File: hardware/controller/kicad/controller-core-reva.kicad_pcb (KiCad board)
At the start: 2 copper layers, 141.6 x 135.2 mm, 158 parts, among them J101 12V_ISOLATED_INPUT / JST XH, J102 STM_SWD / 1x6 2.54mm, J103 ESP_UART / 1x6 2.54mm, J104 UI_LINK / IDC 2x8 2.54mm, J105 JP13 NTC / 2 vías, J106 JP5 FLOW ADAPTER / VCC-GND-OC, J107 JP14 DOOR / contacto seco, J108 JP16 VISUAL V1..V8 / XH-8, J109 JP22 WATER / RED-WHITE-BLACK, J110 USB-C SERVICE / USB 2.0, J111 USB BENCH POWER / OPEN, J112 24V_ACTUATOR_INPUT / JST XH, J113 JP3 VALVE / JST XH, J114 POWER MONITOR / MEASURE ONLY, J115 JP8 GRINDER / 320VDC, J117 JP24 PUMP / 230VAC, J118 JP17 MAINS / L-N, J121 24V INTERNAL SELECT / OPEN FO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, K701 G5RL-1A-E-TV8 DC24, Q501 SI2308A, Q701 SI2308A / relay coil, U101 STM32G431RBT6, U201 ESP32-S3-WROOM-1U-N8R8, U203 USBLC6-2SC6, U301 AP63203WU-7, U302 TPS22918DBVR, U303 AP63200WU-7 / 24V to 12V, U501 DRV8876PWPR, U502 UCC27517DBVR, U601 TPS3828-33DBVR, U602 SN74LVC2G08DCTR, U603 SN74LVC2G08DCTR

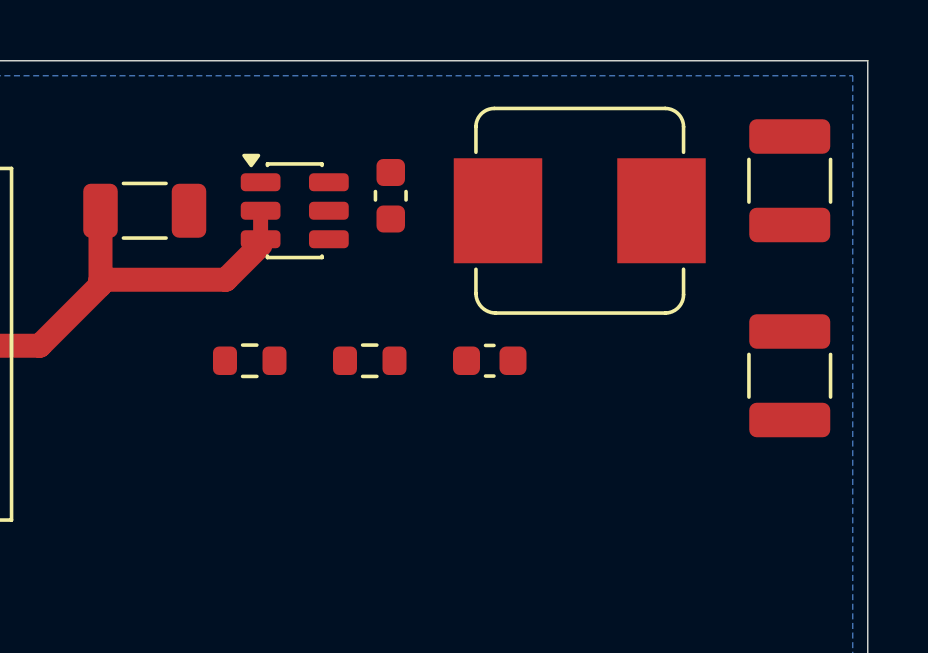
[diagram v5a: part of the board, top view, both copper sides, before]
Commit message: Route the 12 V buck and document the routed blocks
Route the switch node, output bank and divider chain of the AP63200 stage; the
1210 output capacitors share a column with a ground pad, so the rail rounds
them on the inner side. Leave the feedback leg from U303 pin 1 to R302 open and
say why: the 24 V lane wraps round C310 to reach the input pins, leaving only
the channel under the switcher, next to the switch node.

Document every hand-routed block, the reserved reset channel, the back-layer
hops under the power trunks, and two findings: U603 has no decoupling capacitor
of its own, and the SN74LVC2G08 in the DCT package really does carry 2Y on pin
3, which the generator's symbol already matches. DRC clean; 155 connections
remain, down from 273.

Co-Authored-By: Claude Opus 5 <noreply@anthropic.com>
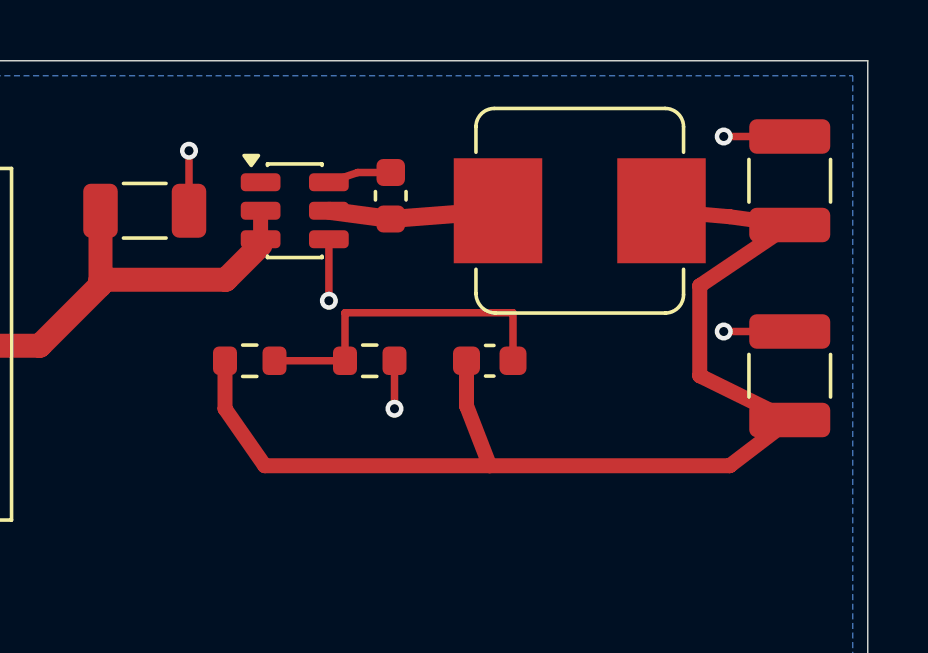
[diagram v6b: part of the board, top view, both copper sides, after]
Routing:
- net /12V_ISO_RAW: track 0.00 -> 39.4 mm
- net /BUCK12_FB: track 0.00 -> 11.2 mm
- net /GND_UI: track 91.9 -> 102.0 mm, vias 56 -> 61
- net /BUCK12_SW: track 0.00 -> 5.67 mm
- net /BUCK12_BST: track 0.00 -> 2.12 mm

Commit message: Give U603 decoupling and the 12 V feedback a clean path
Add C603, a 100 nF beside U603 between it and Q701. The gate that arms mains
was the only logic part without local decoupling, so a supply dip could have
read as a valid high on its inputs.

Move the 12 V feedback divider from below the switcher to the top edge,
north-west of it. Below the switcher it had no route at all: the 24 V lane
wraps round C310 at y = 7.3 mm to reach the input pins, leaving only the
0.95 mm channel under the chip, beside the switch node. R302, R303 and C314 now
share one line at y = 3.4 mm into pin 1 that never meets the lane, and the
divider's top end returns to the inductor pad on a no-current sense line along
the board edge.

ERC passes at 159 components. DRC clean; 154 connections remain.

Co-Authored-By: Claude Opus 5 <noreply@anthropic.com>
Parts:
- added C603: 100nF / arm gate local, Capacitor_SMD:C_0603_1608Metric, F.Cu at (31.5, 75.6)
- moved R303 18.7 mm to (108.0, 2.20), turned to 180 degrees
- moved C314 14.3 mm to (117.0, 2.20)
- moved R302 11.2 mm to (113.0, 2.20)
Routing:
- net /BUCK12_FB: track 11.2 -> 14.4 mm
- net /3V3_CORE: track 83.8 -> 85.6 mm
- net /12V_ISO_RAW: track 39.4 -> 40.9 mm
- net /GND_UI: track 102.0 -> 102.4 mm, vias 61 -> 62

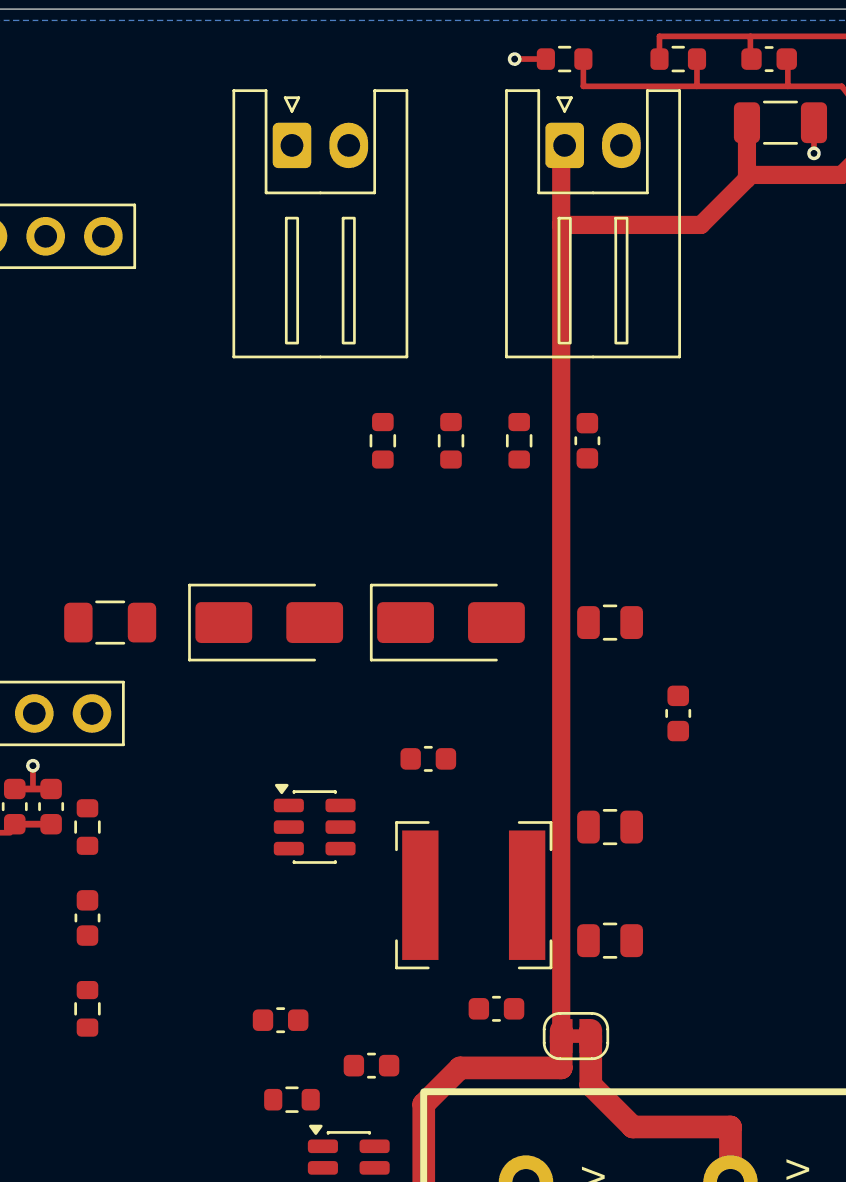
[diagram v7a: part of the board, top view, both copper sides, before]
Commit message: Route the 3.3 V buck and the 12 V telemetry
Move C302 under the switcher so the input loop closes across the package
instead of reaching 8 mm to the bulk capacitor, and take the ground pin to the
plane through that capacitor's own pad.

Move the 24 V lane from x = 107.85 mm to the empty column at x = 112.5 mm. It
used to climb between the inductor and the output capacitors, so every 3.3 V
link crossed it; the capacitors now stay beside the inductor where they belong
and J112 is fed by a short branch.

Route 12V_FUSED over the diodes and 12V_PROTECTED under them, the switch and
bootstrap nodes, the 3.3 V output bank, the sense line back to pin 1 round the
north of the switcher, and the 12 V telemetry divider with R702 turned so the
filtered node runs straight to R703 and C701.

DRC clean; 128 connections remain, down from 154.

Co-Authored-By: Claude Opus 5 <noreply@anthropic.com>
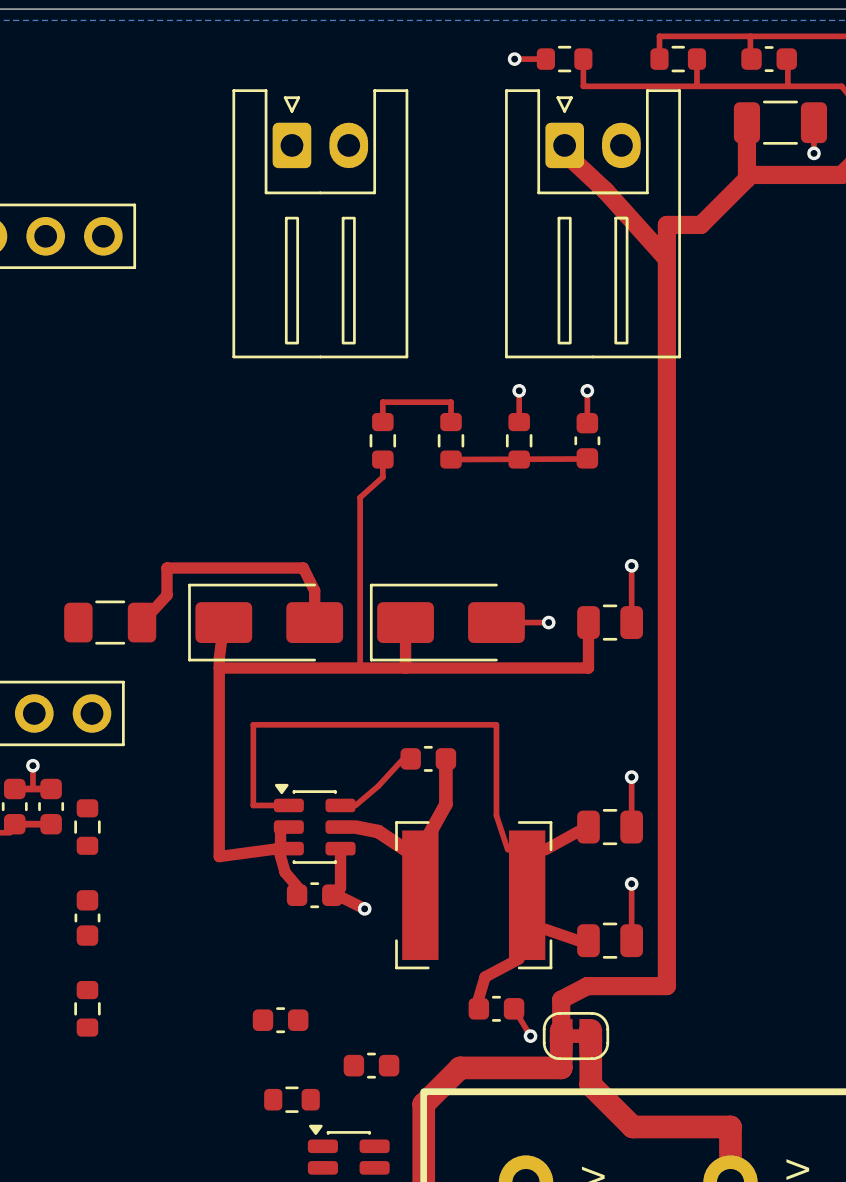
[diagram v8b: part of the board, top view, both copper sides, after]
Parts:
- moved C302 17.9 mm to (97.0, 39.0), turned to 0 degrees
- turned R702 to -90 degrees
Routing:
- net /12V_PROTECTED: track 9.58 -> 53.4 mm
- net /3V3_CORE: track 85.6 -> 112.4 mm
- net /GND_UI: track 102.4 -> 119.2 mm, vias 62 -> 70
- net /12V_FUSED: track 0.00 -> 11.3 mm
- net /SW_NODE: track 0.00 -> 6.06 mm
- net /RAIL_12V_ADC: track 0.00 -> 6.00 mm
- net /RAIL_12V_DIV: track 0.00 -> 4.75 mm
- net /BST_NODE: track 0.00 -> 2.94 mm
- net /24V_ACT_RAW: track 251.3 -> 253.4 mm
